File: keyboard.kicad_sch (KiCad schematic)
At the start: 182 parts

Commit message: Added: + Libraries for Symbols and Footprints + STM32L412 Symbol and Footprint + Hierachical sheets: key_matrix.kicad_sch, supply.kicad_sch
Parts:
- removed D_0, D_1, D_10, D_11, D_12, D_13, D_14, D_15, D_16, D_17, D_18, D_19, D_2, D_20, D_21, D_22, D_23, D_24, D_25, D_26, D_27, D_28, D_29, D_3, D_30, D_31, D_32, D_33, D_34, D_35, D_36, D_37, D_38, D_39, D_4, D_40, D_41, D_42, D_43, D_44, D_45, D_46, D_47, D_48, D_49, D_5, D_50, D_51, D_52, D_53, D_54, D_55, D_56, D_57, D_58, D_59, D_6, D_60, D_61, D_62, D_63, D_64, D_65, D_66, D_67, D_68, D_69, D_7, D_70, D_71, D_72, D_73, D_74, D_75, D_76, D_77, D_78, D_79, D_8, D_80, D_81, D_82, D_83, D_84, D_85, D_86, D_87, D_88, D_89, D_9, D_90: D, Diode_SMD:D_SOD-123, symbol Device:D_Small
- removed K_0, K_1, K_10, K_11, K_12, K_13, K_14, K_15, K_16, K_17, K_18, K_19, K_2, K_20, K_21, K_22, K_23, K_24, K_25, K_26, K_27, K_28, K_3, K_30, K_31, K_32, K_34, K_35, K_36, K_37, K_38, K_39, K_4, K_40, K_41, K_42, K_43, K_44, K_45, K_47, K_48, K_49, K_5, K_51, K_52, K_53, K_54, K_55, K_56, K_57, K_58, K_59, K_6, K_60, K_61, K_62, K_63, K_64, K_65, K_67, K_68, K_69, K_7, K_70, K_71, K_72, K_73, K_74, K_75, K_76, K_77, K_79, K_8, K_88, K_89, K_9, K_90: KEYSW, MX_Alps_Hybrid:MX-1U-NoLED, symbol MX_Alps_Hybrid:MX-NoLED
- removed K_29: KEYSW, MX_Alps_Hybrid:MX-2U-NoLED, symbol MX_Alps_Hybrid:MX-NoLED
- removed K_33: KEYSW, MX_Alps_Hybrid:MX-1.5U-NoLED, symbol MX_Alps_Hybrid:MX-NoLED
- removed K_46, K_66, K_80, K_81, K_82, K_84, K_85, K_86, K_87: KEYSW, MX_Alps_Hybrid:MX-1.25U-NoLED, symbol MX_Alps_Hybrid:MX-NoLED
- removed K_50: KEYSW, MX_Alps_Hybrid:MX-1.75U-NoLED, symbol MX_Alps_Hybrid:MX-NoLED
- removed K_78: KEYSW, MX_Alps_Hybrid:MX-2.75U-NoLED, symbol MX_Alps_Hybrid:MX-NoLED
- removed K_83: KEYSW, MX_Alps_Hybrid:MX-6.25U-NoLED, symbol MX_Alps_Hybrid:MX-NoLED
- added IC?: STM32L412C8U6, CustomKeyboard:QFN50P700X700X65-49N-D, symbol CustomKeyboard:STM32L412C8U6
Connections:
- new net EXT_XTAL32_IN: IC?.3 (PC14/OSC32_IN)
- new net EXT_XTAL32_OUT: IC?.4 (PC15/OSC32_OUT)
- new net EXT_XTAL_IN: IC?.5 (PH0/OSC_IN)
- new net EXT_XTAL_OUT: IC?.6 (PH1/OSC_OUT)
- new net GND: IC?.23 (VSS_1), IC?.35 (VSS_2), IC?.47 (VSS_3), IC?.49 (EP), IC?.8 (VSSA)
- new net NRST: IC?.7 (NRST)
- new net VBAT_EXT: IC?.1 (VBAT)
- new net VDD: IC?.24 (VDD_1), IC?.48 (VDD_2)
- new net VDDA: IC?.9 (VDDA)
- new net VDDUSB_EXT: IC?.36 (VDDUSB)
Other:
- added sheet key_matrix (key_matrix.kicad_sch)
- added sheet supply (supply.kicad_sch)
- note added: "Notes: VBAT operation: is automatically activated if VDD is not present. Internal VBAT battery charging circuit is embedded and activated when VDD is present."
- note added: "TODO: - Supply + Switching Regulator + Input Connector"

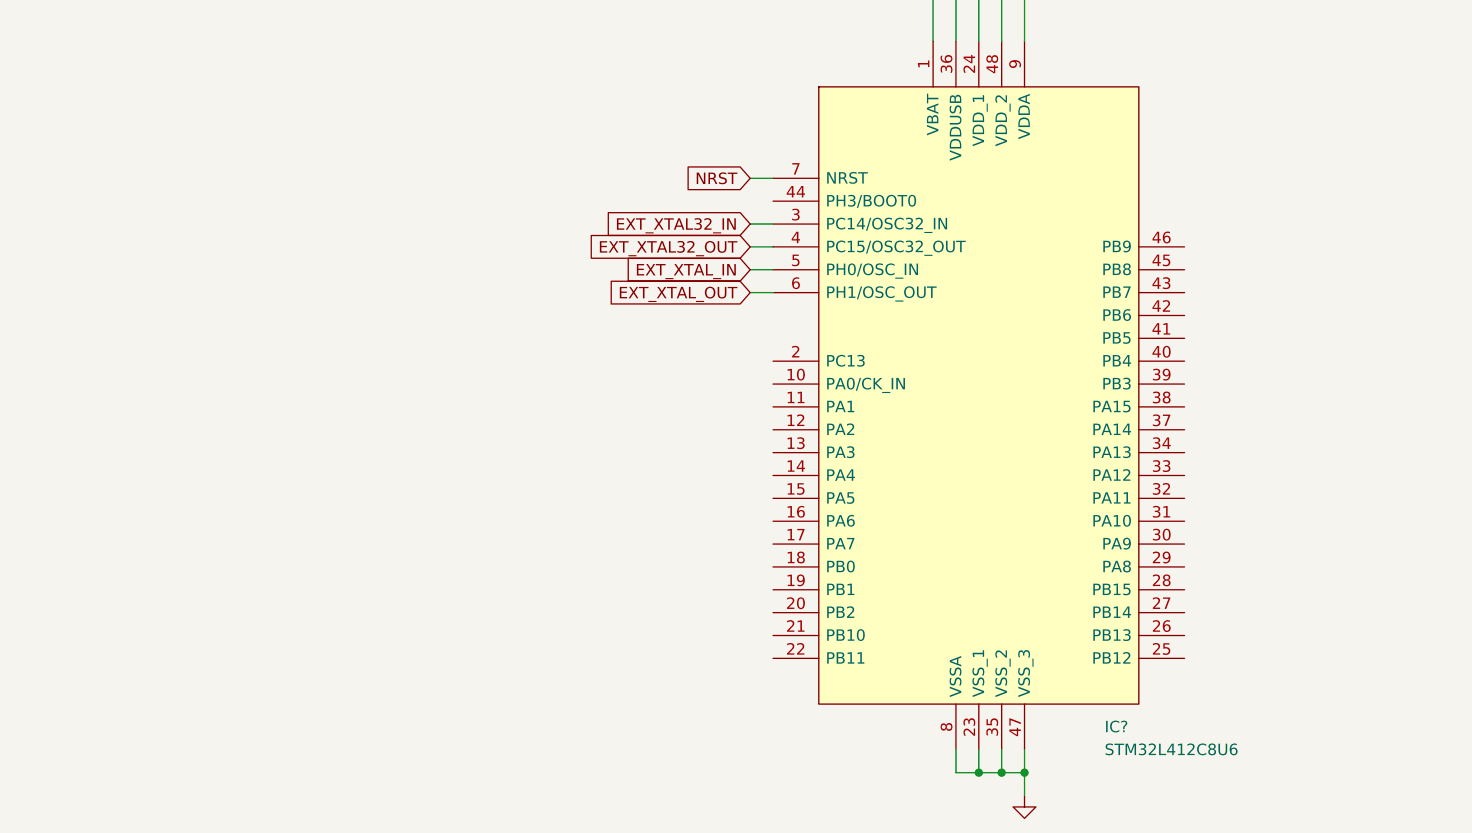
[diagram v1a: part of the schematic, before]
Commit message: Add initial connector pin assignment
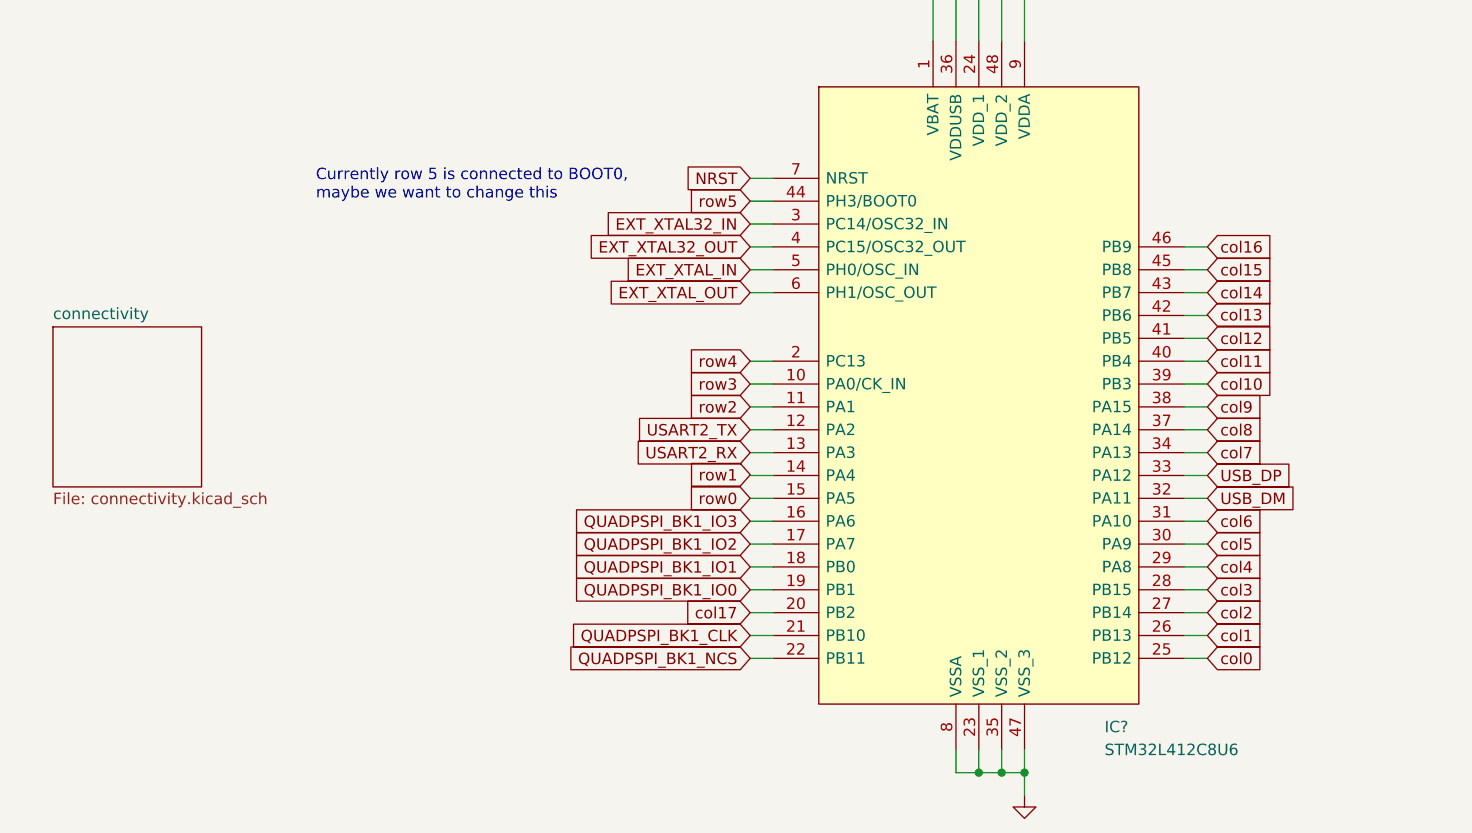
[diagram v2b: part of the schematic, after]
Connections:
- net row3: now reaches IC?.10 (PA0/CK_IN)
- net row2: now reaches IC?.11 (PA1)
- net USART2_TX: now reaches IC?.12 (PA2)
- net USART2_RX: now reaches IC?.13 (PA3)
- net row0: now reaches IC?.15 (PA5)
- net QUADPSPI_BK1_IO3: now reaches IC?.16 (PA6)
- net QUADPSPI_BK1_IO2: now reaches IC?.17 (PA7)
- net QUADPSPI_BK1_IO1: now reaches IC?.18 (PB0)
- net QUADPSPI_BK1_IO0: now reaches IC?.19 (PB1)
- net row4: now reaches IC?.2 (PC13)
- net col17: now reaches IC?.20 (PB2)
- net QUADPSPI_BK1_CLK: now reaches IC?.21 (PB10)
- net QUADPSPI_BK1_NCS: now reaches IC?.22 (PB11)
- net col0: now reaches IC?.25 (PB12)
- net col1: now reaches IC?.26 (PB13)
- net col2: now reaches IC?.27 (PB14)
- net col3: now reaches IC?.28 (PB15)
- net col4: now reaches IC?.29 (PA8)
- net col5: now reaches IC?.30 (PA9)
- net col6: now reaches IC?.31 (PA10)
- net USB_DM: now reaches IC?.32 (PA11)
- net USB_DP: now reaches IC?.33 (PA12)
- net col7: now reaches IC?.34 (PA13)
- net col8: now reaches IC?.37 (PA14)
- net col9: now reaches IC?.38 (PA15)
- net col10: now reaches IC?.39 (PB3)
- net col11: now reaches IC?.40 (PB4)
- net col12: now reaches IC?.41 (PB5)
- net col14: now reaches IC?.43 (PB7)
- net row5: now reaches IC?.44 (PH3/BOOT0)
- net col15: now reaches IC?.45 (PB8)
- net col16: now reaches IC?.46 (PB9)
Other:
- added sheet connectivity (connectivity.kicad_sch)
- note added: "Currently row 5 is connected to BOOT0, maybe we want to change this"

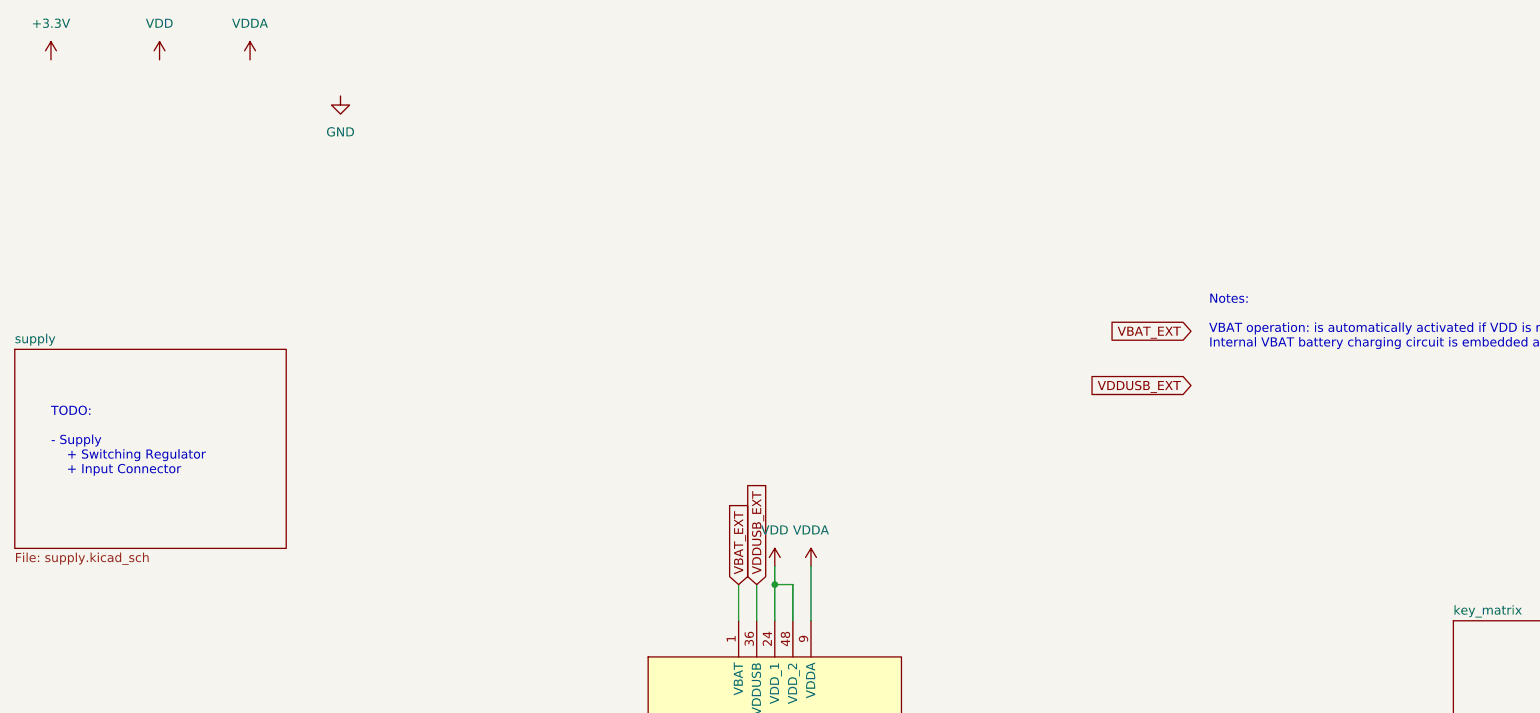
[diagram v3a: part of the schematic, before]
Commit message: Supply: - Added voltage regulator - appended calculations for L and Voltage divider - Added USB-C connector symbol and connected D+/D- lines
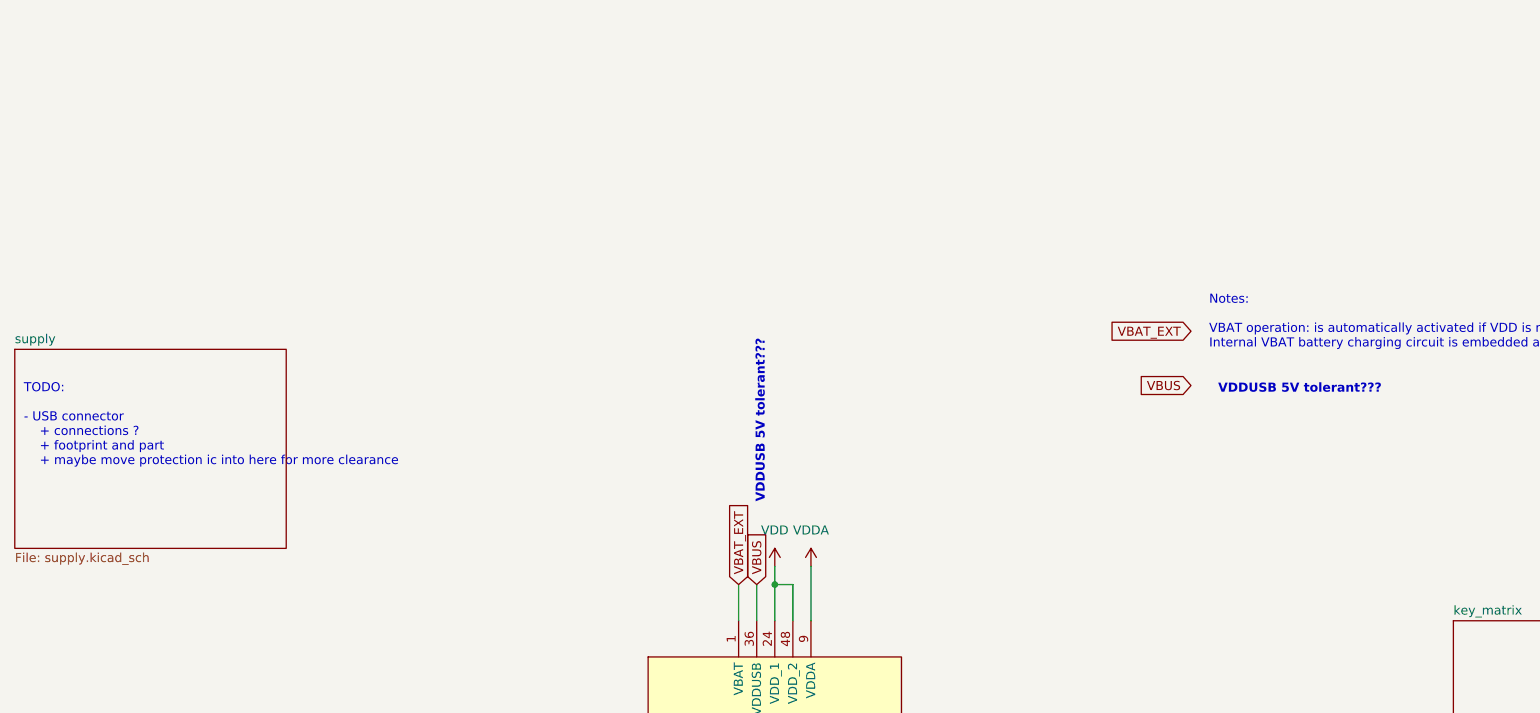
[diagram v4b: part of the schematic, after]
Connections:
- net VDDUSB_EXT renamed VBUS
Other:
- note added: "TODO: - USB connector + connections ? + footprint and part + maybe move protection ic into here for more clearance"
- note added: "VDDUSB 5V tolerant???"
- note removed: "TODO: - Supply + Switching Regulator + Input Connector"
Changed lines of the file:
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@@
     (effects (font (size 1.27 1.27)) (justify left bottom))
   )
-  (text "TODO:\n\n- Supply\n    + Switching Regulator\n    + Input Connector"
-    (at 30.48 43.18 0)
+  (text "VDDUSB 5V tolerant???" (at 130.81 46.99 90)
+    (effects (font (size 1.27 1.27) (thickness 0.254) bold) (justify left bottom))
+  )
+  (text "TODO:\n\n- USB connector\n    + connections ? \n    + footprint and part\n    + maybe move protection ic into here for more clearance"
+    (at 26.67 41.91 0)
     (effects (font (size 1.27 1.27)) (justify left bottom))
   )
+  (text "VDDUSB 5V tolerant???" (at 194.31 31.75 0)
+    (effects (font (size 1.27 1.27) (thickness 0.254) bold) (justify left bottom))
+  )
   (global_label "row1" (shape input) (at 106.6892 111.6776 180) (fields_autoplaced)
     (effects (font (size 1.27 1.27)) (justify right))
@@
     )
   )
-  (global_label "VDDUSB_EXT" (shape input) (at 129.54 58.42 90) (fields_autoplaced)
+  (global_label "VBUS" (shape input) (at 129.54 58.42 90) (fields_autoplaced)
     (effects (font (size 1.27 1.27)) (justify left))
     (property "Intersheet References" "${INTERSHEET_REFS}" (id 0) (at 129.6194 44.3634 90)
@@
     )
   )
-  (global_label "VDDUSB_EXT" (shape input) (at 190.5 30.48 180) (fields_autoplaced)
+  (global_label "VBUS" (shape input) (at 190.5 30.48 180) (fields_autoplaced)
     (effects (font (size 1.27 1.27)) (justify right))
     (property "Intersheet References" "${INTERSHEET_REFS}" (id 0) (at 176.4434 30.4006 0)
@@
     )
     (property "Datasheet" "" (id 3) (at 137.16 147.32 0)
-      (effects (font (size 1.27 1.27)) hide)
-    )
-    (pin "1")
-  )
-  (symbol (lib_id "power:VDD") (at 45.72 -15.24 0) (unit 1)
-    (in_bom yes) (on_board yes) (fields_autoplaced)
-    (property "Reference" "#PWR?" (id 0) (at 45.72 -11.43 0)
-      (effects (font (size 1.27 1.27)) hide)
-    )
-    (property "Value" "VDD" (id 1) (at 45.72 -20.32 0))
-    (property "Footprint" "" (id 2) (at 45.72 -15.24 0)
-      (effects (font (size 1.27 1.27)) hide)
-    )
-    (property "Datasheet" "" (id 3) (at 45.72 -15.24 0)
-      (effects (font (size 1.27 1.27)) hide)
-    )
-    (pin "1")
-  )
-  (symbol (lib_id "power:+3.3V") (at 30.48 -15.24 0) (unit 1)
-    (in_bom yes) (on_board yes) (fields_autoplaced)
-    (property "Reference" "#PWR?" (id 0) (at 30.48 -11.43 0)
-      (effects (font (size 1.27 1.27)) hide)
-    )
-    (property "Value" "+3.3V" (id 1) (at 30.48 -20.32 0))
-    (property "Footprint" "" (id 2) (at 30.48 -15.24 0)
-      (effects (font (size 1.27 1.27)) hide)
-    )
-    (property "Datasheet" "" (id 3) (at 30.48 -15.24 0)
-      (effects (font (size 1.27 1.27)) hide)
-    )
-    (pin "1")
-  )
-  (symbol (lib_id "power:VDDA") (at 58.42 -15.24 0) (unit 1)
-    (in_bom yes) (on_board yes) (fields_autoplaced)
-    (property "Reference" "#PWR?" (id 0) (at 58.42 -11.43 0)
-      (effects (font (size 1.27 1.27)) hide)
-    )
-    (property "Value" "VDDA" (id 1) (at 58.42 -20.32 0))
-    (property "Footprint" "" (id 2) (at 58.42 -15.24 0)
-      (effects (font (size 1.27 1.27)) hide)
-    )
-    (property "Datasheet" "" (id 3) (at 58.42 -15.24 0)
       (effects (font (size 1.27 1.27)) hide)
     )
@@
     (pin "9")
   )
-  (symbol (lib_id "power:GND") (at 71.12 -10.16 0) (unit 1)
-    (in_bom yes) (on_board yes) (fields_autoplaced)
-    (property "Reference" "#PWR?" (id 0) (at 71.12 -3.81 0)
-      (effects (font (size 1.27 1.27)) hide)
-    )
-    (property "Value" "GND" (id 1) (at 71.12 -5.08 0))
-    (property "Footprint" "" (id 2) (at 71.12 -10.16 0)
-      (effects (font (size 1.27 1.27)) hide)
-    )
-    (property "Datasheet" "" (id 3) (at 71.12 -10.16 0)
-      (effects (font (size 1.27 1.27)) hide)
-    )
-    (pin "1")
-  )
   (symbol (lib_id "power:VDD") (at 132.08 55.88 0) (unit 1)
     (in_bom yes) (on_board yes) (fields_autoplaced)
@@
       (reference "#PWR?") (unit 1) (value "GND") (footprint "")
     )
+    (path "/2e76080d-00c4-4f0f-a613-1d146ef507ec/138ba9ef-9528-4e96-a8ed-d774f7a35042"
+      (reference "#PWR?") (unit 1) (value "GND") (footprint "")
+    )
     (path "/f594353b-e230-4906-a36a-eccbf7cb4bea/1cd76bdf-57b6-410e-85df-cab522615b04"
       (reference "#PWR?") (unit 1) (value "GND") (footprint "")
     )
+    (path "/2e76080d-00c4-4f0f-a613-1d146ef507ec/256714b1-4bbf-4d41-816e-ccc1c87f9805"
+      (reference "#PWR?") (unit 1) (value "GND") (footprint "")
+    )
     (path "/3242e991-ee59-4165-8a71-02cb3a269b1a"
       (reference "#PWR?") (unit 1) (value "GND") (footprint "")
-    )
-    (path "/3b08d33e-9dc4-403c-8918-3701bf2162b2"
-      (reference "#PWR?") (unit 1) (value "VDD") (footprint "")
     )
     (path "/2e76080d-00c4-4f0f-a613-1d146ef507ec/4b31b3fe-ddce-4cd9-a842-82cb3fa8825d"
@@
       (reference "#PWR?") (unit 1) (value "+3.3V") (footprint "")
     )
-    (path "/74f1228a-6d3b-41ac-a556-f9e547cbff5c"
-      (reference "#PWR?") (unit 1) (value "+3.3V") (footprint "")
-    )
-    (path "/8e8534a8-2a6b-4596-b0a8-1733a496a817"
-      (reference "#PWR?") (unit 1) (value "VDDA") (footprint "")
+    (path "/2e76080d-00c4-4f0f-a613-1d146ef507ec/63db89db-772e-45dd-8b57-2816c9e77877"
+      (reference "#PWR?") (unit 1) (value "GND") (footprint "")
     )
     (path "/f594353b-e230-4906-a36a-eccbf7cb4bea/99cf359e-5050-4ce2-8891-a49476ae23f1"
+      (reference "#PWR?") (unit 1) (value "GND") (footprint "")
+    )
+    (path "/2e76080d-00c4-4f0f-a613-1d146ef507ec/a5c2b7db-d7df-400d-9910-37e11c152f3a"
       (reference "#PWR?") (unit 1) (value "GND") (footprint "")
     )
@@
       (reference "#PWR?") (unit 1) (value "VDD") (footprint "")
     )
-    (path "/2e76080d-00c4-4f0f-a613-1d146ef507ec/bd2efa74-2789-477c-93c2-0f54e8bbc7c2"
+    (path "/2e76080d-00c4-4f0f-a613-1d146ef507ec/d665e935-2e54-4fa1-a922-56c8e6a56f0d"
       (reference "#PWR?") (unit 1) (value "+3.3V") (footprint "")
     )
-    (path "/dc711d79-70d0-4fbc-9d3b-371a55d535d1"
+    (path "/2e76080d-00c4-4f0f-a613-1d146ef507ec/e6905c38-efcd-4439-8a8a-736cb36a037a"
       (reference "#PWR?") (unit 1) (value "GND") (footprint "")
     )
@@
       (reference "C?") (unit 1) (value "4.7u") (footprint "Capacitor_SMD:C_0603_1608Metric")
     )
+    (path "/2e76080d-00c4-4f0f-a613-1d146ef507ec/915babe6-586a-497c-8db7-a914655f8401"
+      (reference "C?") (unit 1) (value "10u") (footprint "Capacitor_SMD:C_0603_1608Metric")
+    )
     (path "/2e76080d-00c4-4f0f-a613-1d146ef507ec/924e486f-b5eb-463f-a9e2-2a7aa9fa2d5e"
       (reference "C?") (unit 1) (value "10n") (footprint "Capacitor_SMD:C_0603_1608Metric")
     )
+    (path "/2e76080d-00c4-4f0f-a613-1d146ef507ec/c59c5cb1-6a8a-40bc-a332-3e2c2133fb27"
+      (reference "C?") (unit 1) (value "22u") (footprint "Capacitor_SMD:C_0603_1608Metric")
+    )
     (path "/2e76080d-00c4-4f0f-a613-1d146ef507ec/e88b5274-bb38-446d-a378-c22bc95d5372"
       (reference "C?") (unit 1) (value "100n") (footprint "Capacitor_SMD:C_0603_1608Metric")
@@
       (reference "IC?") (unit 1) (value "STM32L412C8U6") (footprint "CustomKeyboard:QFN50P700X700X65-49N-D")
     )
+    (path "/2e76080d-00c4-4f0f-a613-1d146ef507ec/da1a5235-6806-4dcf-8db2-ffbc26bdd040"
+      (reference "IC?") (unit 1) (value "MP2152GTF-Z") (footprint "CustomKeyboard:MP2152GTF33P")
+    )
     (path "/f594353b-e230-4906-a36a-eccbf7cb4bea/aa1e8f35-586d-4b2a-a879-91ed1e27cbc9"
       (reference "J?") (unit 1) (value "ESP8266_Conn") (footprint "")
@@
       (reference "K_?") (unit 1) (value "KEYSW") (footprint "MX_Alps_Hybrid:MX-1U-NoLED")
     )
+    (path "/2e76080d-00c4-4f0f-a613-1d146ef507ec/623e84a4-f0e7-4ba9-9d5a-9b1134a8c4f8"
+      (reference "L?") (unit 1) (value "33u / 2A") (footprint "")
+    )
+    (path "/2e76080d-00c4-4f0f-a613-1d146ef507ec/8595e358-e4f7-4e90-b516-47fe5f442207"
+      (reference "P?") (unit 1) (value "USB_C_Plug_USB2.0") (footprint "")
+    )
+    (path "/2e76080d-00c4-4f0f-a613-1d146ef507ec/5b8a3099-610d-4fdf-b56f-bf8e6ecc274f"
+      (reference "R?") (unit 1) (value "68k") (footprint "Resistor_SMD:R_0603_1608Metric")
+    )
+    (path "/2e76080d-00c4-4f0f-a613-1d146ef507ec/95941dc7-d093-4f6d-ab2e-b0ee90e347ad"
+      (reference "R?") (unit 1) (value "15k") (footprint "")
+    )
     (path "/f594353b-e230-4906-a36a-eccbf7cb4bea/ab7dda6c-8731-437a-9286-303f5200309e"
